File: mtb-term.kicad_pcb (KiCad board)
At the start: 2 copper layers, 22 x 14.5 mm, 10 parts, among them J1 Conn_01x04, U1 L78L05_SOT89

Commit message: Add PCB description text.
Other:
- board text added: "RS485 term v1.0 JH 2021"
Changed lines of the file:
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@@
   (general
     (thickness 1.6)
-    (drawings 12)
+    (drawings 13)
     (tracks 30)
     (zones 0)
@@
       (effects (font (size 1 1) (thickness 0.15)))
     )
-    (fp_text user %R (at 0 0 90) (layer F.Fab)
-      (effects (font (size 0.5 0.5) (thickness 0.08)))
-    )
-    (fp_line (start -1 0.625) (end -1 -0.625) (layer F.Fab) (width 0.1))
-    (fp_line (start -1 -0.625) (end 1 -0.625) (layer F.Fab) (width 0.1))
-    (fp_line (start 1 -0.625) (end 1 0.625) (layer F.Fab) (width 0.1))
-    (fp_line (start 1 0.625) (end -1 0.625) (layer F.Fab) (width 0.1))
-    (fp_line (start -0.227064 -0.735) (end 0.227064 -0.735) (layer F.SilkS) (width 0.12))
-    (fp_line (start -0.227064 0.735) (end 0.227064 0.735) (layer F.SilkS) (width 0.12))
-    (fp_line (start -1.68 0.95) (end -1.68 -0.95) (layer F.CrtYd) (width 0.05))
-    (fp_line (start -1.68 -0.95) (end 1.68 -0.95) (layer F.CrtYd) (width 0.05))
-    (fp_line (start 1.68 -0.95) (end 1.68 0.95) (layer F.CrtYd) (width 0.05))
-    (fp_line (start 1.68 0.95) (end -1.68 0.95) (layer F.CrtYd) (width 0.05))
+    (fp_line (start -1 0.625) (end -1 -0.625) (layer F.Fab) (width 0.1))
+    (fp_line (start -1 -0.625) (end 1 -0.625) (layer F.Fab) (width 0.1))
+    (fp_line (start 1 -0.625) (end 1 0.625) (layer F.Fab) (width 0.1))
+    (fp_line (start 1 0.625) (end -1 0.625) (layer F.Fab) (width 0.1))
+    (fp_line (start -0.227064 -0.735) (end 0.227064 -0.735) (layer F.SilkS) (width 0.12))
+    (fp_line (start -0.227064 0.735) (end 0.227064 0.735) (layer F.SilkS) (width 0.12))
+    (fp_line (start -1.68 0.95) (end -1.68 -0.95) (layer F.CrtYd) (width 0.05))
+    (fp_line (start -1.68 -0.95) (end 1.68 -0.95) (layer F.CrtYd) (width 0.05))
+    (fp_line (start 1.68 -0.95) (end 1.68 0.95) (layer F.CrtYd) (width 0.05))
+    (fp_line (start 1.68 0.95) (end -1.68 0.95) (layer F.CrtYd) (width 0.05))
+    (fp_text user %R (at 0 0 90) (layer F.Fab)
+      (effects (font (size 0.5 0.5) (thickness 0.08)))
+    )
     (pad 1 smd roundrect (at -0.9125 0 90) (size 1.025 1.4) (layers F.Cu F.Paste F.Mask) (roundrect_rratio 0.243902)
       (net 7 "Net-(J1-Pad1)"))
@@
     (fp_text value LED (at 0 1.65 90) (layer F.Fab)
       (effects (font (size 1 1) (thickness 0.15)))
-    )
-    (fp_text user %R (at 0 0 90) (layer F.Fab)
-      (effects (font (size 0.5 0.5) (thickness 0.08)))
     )
     (fp_line (start 1 -0.6) (end -0.7 -0.6) (layer F.Fab) (width 0.1))
@@
     (fp_line (start 1.68 -0.95) (end 1.68 0.95) (layer F.CrtYd) (width 0.05))
     (fp_line (start 1.68 0.95) (end -1.68 0.95) (layer F.CrtYd) (width 0.05))
+    (fp_text user %R (at 0 0 90) (layer F.Fab)
+      (effects (font (size 0.5 0.5) (thickness 0.08)))
+    )
     (pad 1 smd roundrect (at -0.9375 0 270) (size 0.975 1.4) (layers F.Cu F.Paste F.Mask) (roundrect_rratio 0.25)
       (net 5 "Net-(D2-Pad1)"))
@@
     )
   )
+  (gr_text "RS485 term\nv1.0 JH 2021" (at 145.669 87.376) (layer B.SilkS)
+    (effects (font (size 1.5 1.5) (thickness 0.15)) (justify mirror))
+  )
   (gr_arc (start 154.5 93.5) (end 154.5 95.5) (angle -90) (layer Edge.Cuts) (width 0.05))

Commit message: PCB: position values to be readable.
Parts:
- U1: value L78L05_SOT89 -> L78L05

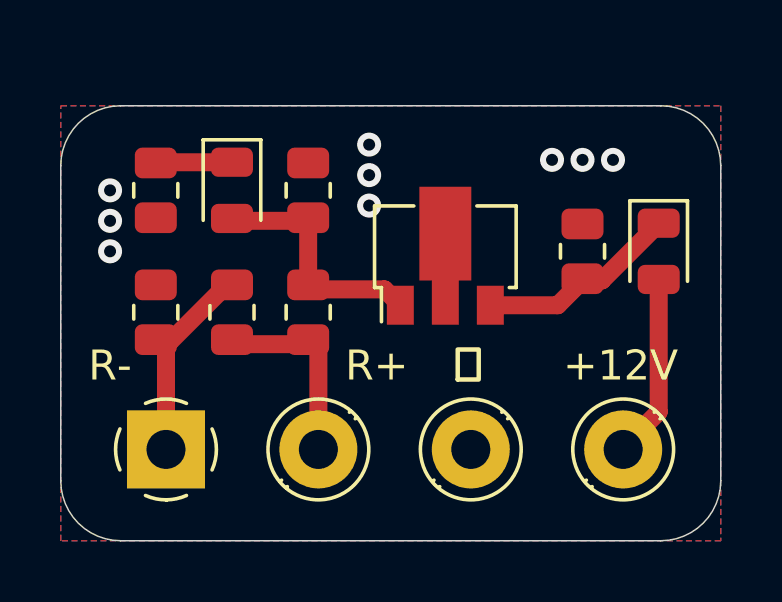
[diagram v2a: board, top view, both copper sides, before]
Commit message: 78L05 hand-soldering package, all holes circular.
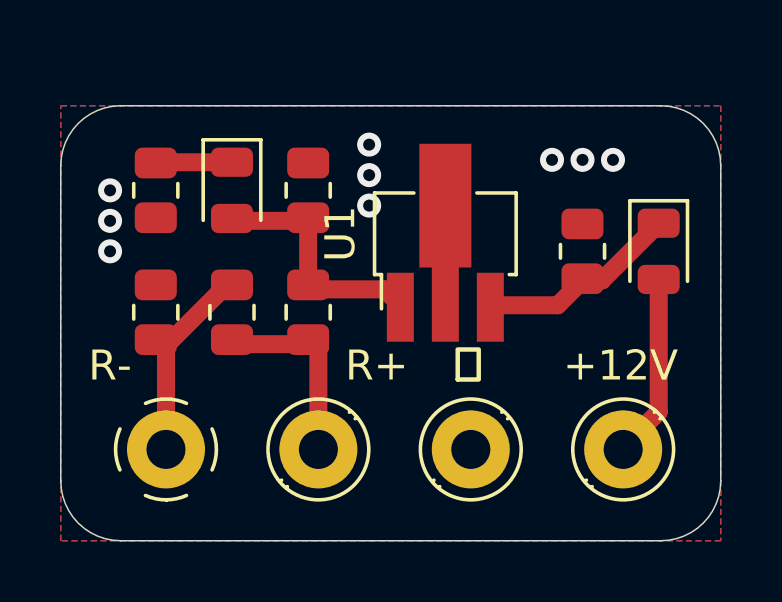
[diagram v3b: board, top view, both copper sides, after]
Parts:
- U1: footprint Package_TO_SOT_SMD:SOT-89-3 -> Package_TO_SOT_SMD:SOT-89-3_Handsoldering
- moved U1 0.43 mm to (147.3, 85.6)

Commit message: Migrate to KiCad 6.
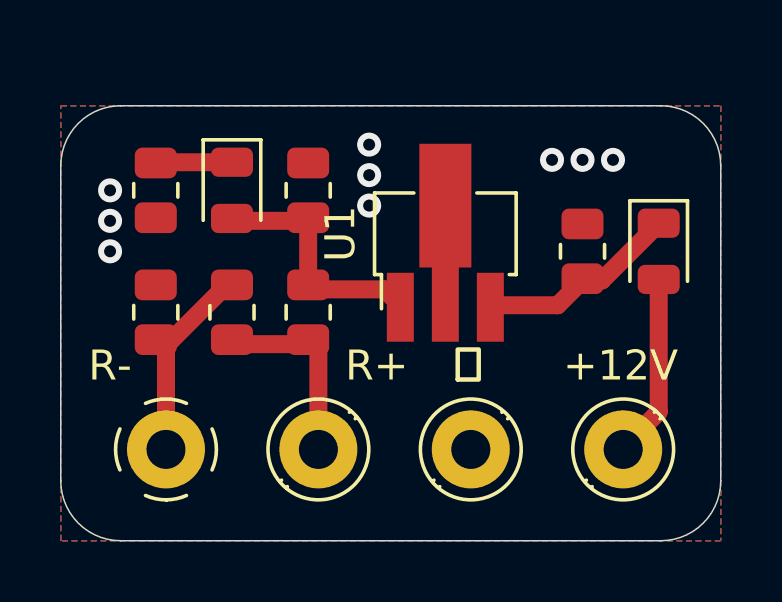
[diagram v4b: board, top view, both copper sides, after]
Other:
- net class Default removed

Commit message: Add TVS.
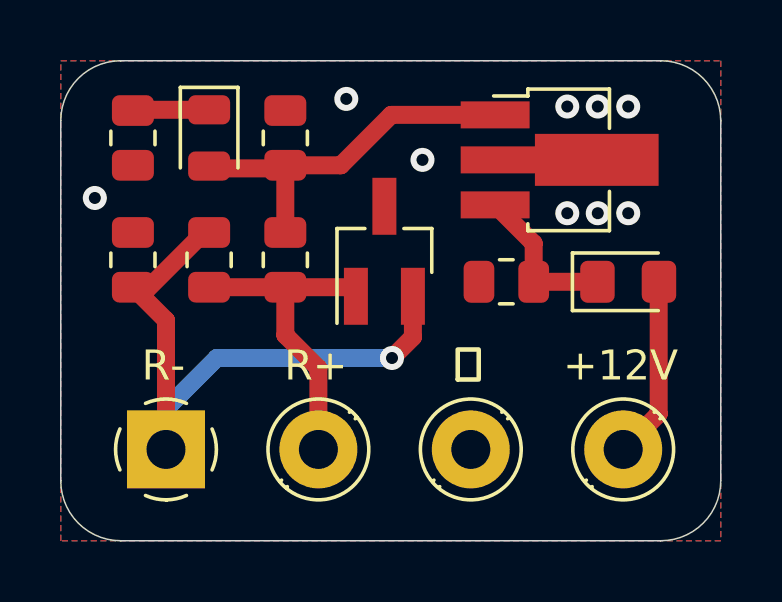
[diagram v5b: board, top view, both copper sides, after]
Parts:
- added D3: SM712_SOT23, Package_TO_SOT_SMD:SOT-23_Handsoldering, F.Cu at (145.3, 85.9)
- D1: footprint Diode_SMD:D_0805_2012Metric -> Diode_SMD:D_0805_2012Metric_Pad1.15x1.40mm_HandSolder
- U1: value L78L05 -> L78L05_SOT89
- moved U1 4.71 mm to (151.1, 82.8), turned to 0 degrees
- moved C1 2.74 mm to (149.4, 86.9), turned to 180 degrees
- moved R2 1.91 mm to (142.0, 86.1)
- moved R3 1.91 mm to (139.4, 86.1)
- moved R4 1.91 mm to (136.9, 86.1)
- moved C2 1.91 mm to (142.0, 82.1)
- moved D2 1.91 mm to (139.4, 82.1)
- moved R1 1.91 mm to (136.9, 82.1)
- moved D1 1.44 mm to (153.4, 86.9), turned to 0 degrees
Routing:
- net Net-(D3-Pad2): track 7.33 -> 21.9 mm, vias 0 -> 1
- net +5V: track 8.12 -> 12.8 mm
- net Net-(D3-Pad1): track 6.34 -> 10.9 mm
- net Net-(C1-Pad1): track 6.96 -> 5.48 mm
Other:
- board size 22 x 14.5 mm -> 22 x 16 mm
- board text added: "RS485 term & TVS v1.1 JH 2022"
- board text removed: "RS485 term v1.0 JH 2021"
